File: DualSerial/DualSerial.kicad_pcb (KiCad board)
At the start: 2 copper layers, 99.9 x 99.9 mm, 22 parts, among them CN1 DB9 Male, CN2 DB9 Male, J1 COM_A_SELECT, J2 IRQ_A_SELECT, J3 COM_A_SELECT, J4 IRQ_B_SELECT, J5 Bus_ISA_8bit, U1 16550/16C550, U2 GAL16V8, U3 GD75232N, U4 1.8432 MHz, U8 16550/16C550, U9 GD75232N

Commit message: Dual Serial: Flip A and B ports to correct location.
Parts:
- J2: renamed from J4; value IRQ_B_SELECT -> IRQ_A_SELECT
- J4: renamed from J2; value IRQ_A_SELECT -> IRQ_B_SELECT
- renumbered C8 to C1, C9 to C3, C1 to C8, C3 to C9, CN2 to CN1, CN1 to CN2, U8 to U1, U9 to U3, U1 to U8, U3 to U9
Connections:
- CN1 pad 1: /SERB_PIN1 -> /SERA_PIN1
- CN1 pad 2: /SERB_PIN2 -> /SERA_PIN2
- CN1 pad 3: /SERB_PIN3 -> /SERA_PIN3
- CN1 pad 4: /SERB_PIN4 -> /SERA_PIN4
- CN1 pad 6: /SERB_PIN6 -> /SERA_PIN6
- CN1 pad 7: /SERB_PIN7 -> /SERA_PIN7
- CN1 pad 8: /SERB_PIN8 -> /SERA_PIN8
- CN1 pad 9: /SERB_PIN9 -> /SERA_PIN9
- CN2 pad 1: /SERA_PIN1 -> /SERB_PIN1
- CN2 pad 2: /SERA_PIN2 -> /SERB_PIN2
- CN2 pad 3: /SERA_PIN3 -> /SERB_PIN3
- CN2 pad 4: /SERA_PIN4 -> /SERB_PIN4
- CN2 pad 6: /SERA_PIN6 -> /SERB_PIN6
- CN2 pad 7: /SERA_PIN7 -> /SERB_PIN7
- CN2 pad 8: /SERA_PIN8 -> /SERB_PIN8
- CN2 pad 9: /SERA_PIN9 -> /SERB_PIN9
- U1 pad 14: ~UART_B_CS -> ~UART_A_CS
- U2 pad 14: ~UART_A_CS -> ~UART_B_CS
- U2 pad 15: ~UART_B_CS -> ~UART_A_CS
- U3 pad 2: /SERB_PIN9 -> /SERA_PIN9
- U3 pad 3: /SERB_PIN8 -> /SERA_PIN8
- U3 pad 4: /SERB_PIN2 -> /SERA_PIN2
- U3 pad 5: /SERB_PIN4 -> /SERA_PIN4
- U3 pad 6: /SERB_PIN3 -> /SERA_PIN3
- U3 pad 7: /SERB_PIN6 -> /SERA_PIN6
- U3 pad 8: /SERB_PIN7 -> /SERA_PIN7
- U3 pad 9: /SERB_PIN1 -> /SERA_PIN1
- U8 pad 14: ~UART_A_CS -> ~UART_B_CS
- U9 pad 2: /SERA_PIN9 -> /SERB_PIN9
- U9 pad 3: /SERA_PIN8 -> /SERB_PIN8
- U9 pad 4: /SERA_PIN2 -> /SERB_PIN2
- U9 pad 5: /SERA_PIN4 -> /SERB_PIN4
- U9 pad 6: /SERA_PIN3 -> /SERB_PIN3
- U9 pad 7: /SERA_PIN6 -> /SERB_PIN6
- U9 pad 8: /SERA_PIN7 -> /SERB_PIN7
- U9 pad 9: /SERA_PIN1 -> /SERB_PIN1
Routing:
- net ~UART_B_CS: track 8.45 -> 43.2 mm, vias 0 -> 2
- net ~UART_A_CS: track 43.2 -> 8.45 mm, vias 2 -> 0
- net /SERB_PIN2: track 24.7 -> 30.1 mm, vias 0 -> 2
- net /SERA_PIN2: track 30.1 -> 24.7 mm, vias 2 -> 0
- net /SERB_PIN8: track 17.9 -> 23.0 mm
- net /SERA_PIN8: track 23.0 -> 17.9 mm
- net /SERB_PIN6: track 16.8 -> 20.5 mm, vias 0 -> 2
- net /SERA_PIN6: track 20.5 -> 16.8 mm, vias 2 -> 0
- net /SERB_PIN7: track 21.3 -> 17.6 mm, vias 2 -> 0
- net /SERA_PIN7: track 17.6 -> 21.3 mm, vias 0 -> 2
- net /SERB_PIN9: track 18.2 -> 21.8 mm
- net /SERA_PIN9: track 21.8 -> 18.2 mm
- net /SERB_PIN1: track 16.5 -> 14.9 mm
- net /SERA_PIN1: track 14.9 -> 16.5 mm
- net /SERB_PIN3: track 15.0 -> 15.8 mm
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
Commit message: Dual Serial: Minor silk screen change.
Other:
- board text added: "COM2:"

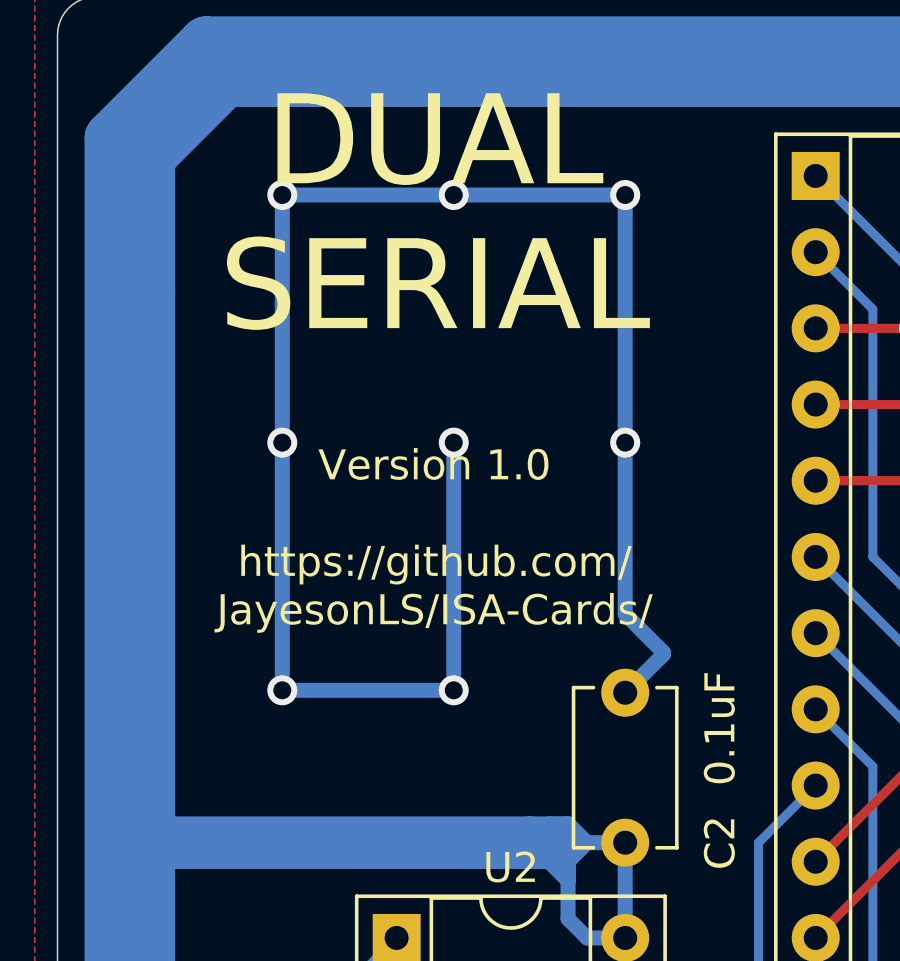
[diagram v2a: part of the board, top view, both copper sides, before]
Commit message: DualSerial: Change to ground plan vias in top left corner.
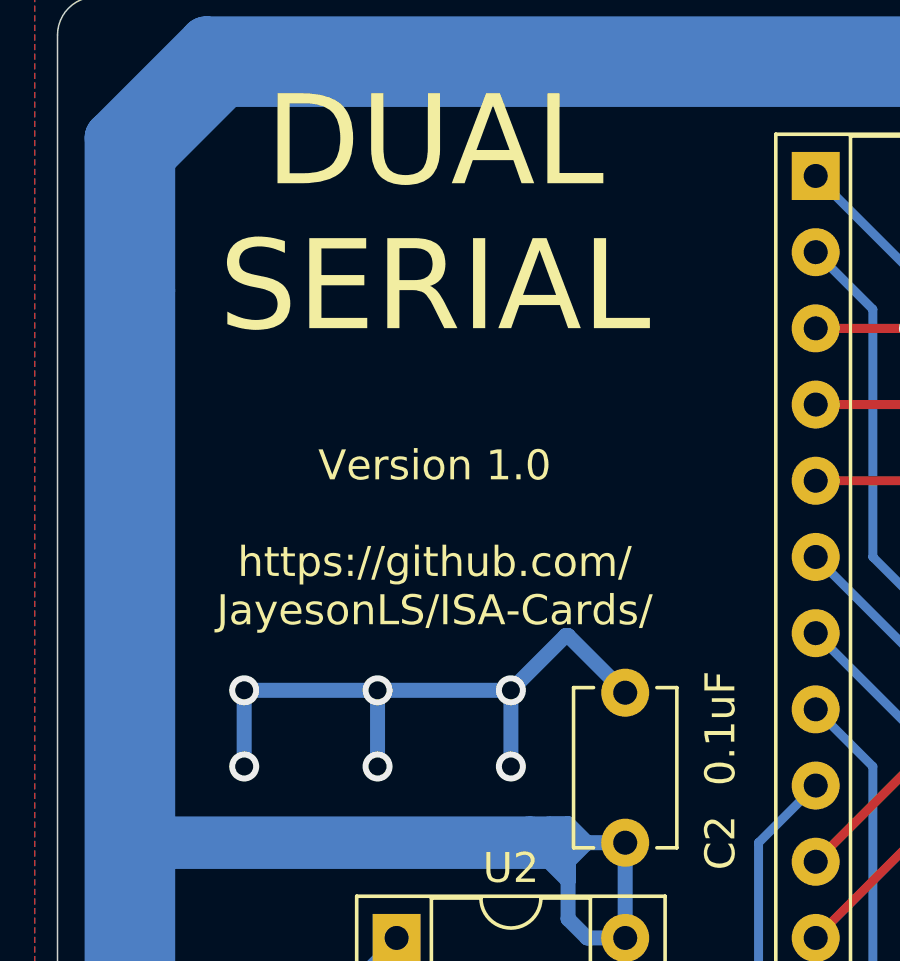
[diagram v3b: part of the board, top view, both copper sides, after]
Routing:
- net GND: track 365.0 -> 327.3 mm, vias 46 -> 44
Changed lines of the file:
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@@
     (thickness 1.6)
     (drawings 87)
-    (tracks 1197)
+    (tracks 1192)
     (zones 0)
     (modules 22)
@@
   (segment (start 173.282894 48.895) (end 170.18 48.895) (width 0.5) (layer B.Cu) (net 20))
   (segment (start 170.18 48.895) (end 166.37 48.895) (width 0.5) (layer B.Cu) (net 20))
-  (via (at 115.57 48.895) (size 1) (drill 0.6) (layers F.Cu B.Cu) (net 20))
-  (segment (start 115.57 48.895) (end 115.57 57.15) (width 0.5) (layer B.Cu) (net 20))
-  (via (at 115.57 57.15) (size 1) (drill 0.6) (layers F.Cu B.Cu) (net 20))
-  (via (at 109.855 57.15) (size 1) (drill 0.6) (layers F.Cu B.Cu) (net 20))
-  (segment (start 109.855 65.405) (end 109.855 57.15) (width 0.5) (layer B.Cu) (net 20))
-  (via (at 109.855 65.405) (size 1) (drill 0.6) (layers F.Cu B.Cu) (net 20))
-  (segment (start 115.57 48.895) (end 109.855 48.895) (width 0.5) (layer B.Cu) (net 20))
-  (via (at 109.855 48.895) (size 1) (drill 0.6) (layers F.Cu B.Cu) (net 20))
-  (segment (start 109.855 48.895) (end 104.14 48.895) (width 0.5) (layer B.Cu) (net 20))
-  (via (at 104.14 48.895) (size 1) (drill 0.6) (layers F.Cu B.Cu) (net 20))
-  (segment (start 104.14 48.895) (end 104.14 57.15) (width 0.5) (layer B.Cu) (net 20))
-  (via (at 104.14 57.15) (size 1) (drill 0.6) (layers F.Cu B.Cu) (net 20))
-  (segment (start 104.14 57.15) (end 104.14 65.405) (width 0.5) (layer B.Cu) (net 20))
-  (segment (start 104.14 65.405) (end 109.855 65.405) (width 0.5) (layer B.Cu) (net 20))
-  (via (at 104.14 65.405) (size 1) (drill 0.6) (layers F.Cu B.Cu) (net 20))
   (segment (start 140.97 53.26) (end 139.78 52.07) (width 0.5) (layer F.Cu) (net 20))
   (segment (start 140.97 53.26) (end 142.16 52.07) (width 0.5) (layer F.Cu) (net 20))
@@
   (segment (start 175.26 54.61) (end 169.545 54.61) (width 0.5) (layer B.Cu) (net 20))
   (segment (start 169.545 54.61) (end 165.1 54.61) (width 0.5) (layer B.Cu) (net 20))
-  (segment (start 115.57 65.485) (end 116.84 64.215) (width 0.5) (layer B.Cu) (net 20))
-  (segment (start 116.84 64.215) (end 116.84 64.135) (width 0.5) (layer B.Cu) (net 20))
-  (segment (start 116.84 64.135) (end 115.57 62.865) (width 0.5) (layer B.Cu) (net 20))
-  (segment (start 115.57 57.15) (end 115.57 62.865) (width 0.5) (layer B.Cu) (net 20))
   (via (at 151.765 64.77) (size 1) (drill 0.6) (layers F.Cu B.Cu) (net 20))
   (segment (start 147.955 64.77) (end 151.765 64.77) (width 0.5) (layer B.Cu) (net 20))
@@
   (segment (start 107.95 100.965) (end 105.41 100.965) (width 0.5) (layer F.Cu) (net 20))
   (segment (start 115.57 107.315) (end 115.57 109.855) (width 0.3) (layer F.Cu) (net 20))
+  (via (at 102.87 65.405) (size 1) (drill 0.6) (layers F.Cu B.Cu) (net 20))
+  (segment (start 113.665 63.58) (end 115.57 65.485) (width 0.5) (layer B.Cu) (net 20))
+  (segment (start 113.585 63.58) (end 113.665 63.58) (width 0.5) (layer B.Cu) (net 20))
+  (segment (start 111.76 65.405) (end 113.585 63.58) (width 0.5) (layer B.Cu) (net 20))
+  (via (at 111.76 65.405) (size 1) (drill 0.6) (layers F.Cu B.Cu) (net 20))
+  (segment (start 107.315 65.405) (end 111.76 65.405) (width 0.5) (layer B.Cu) (net 20))
+  (segment (start 102.87 65.405) (end 107.315 65.405) (width 0.5) (layer B.Cu) (net 20))
+  (via (at 107.315 65.405) (size 1) (drill 0.6) (layers F.Cu B.Cu) (net 20))
+  (via (at 111.76 67.945) (size 1) (drill 0.6) (layers F.Cu B.Cu) (net 20))
+  (segment (start 111.76 65.405) (end 111.76 67.945) (width 0.5) (layer B.Cu) (net 20))
+  (via (at 107.315 67.945) (size 1) (drill 0.6) (layers F.Cu B.Cu) (net 20))
+  (segment (start 107.315 65.405) (end 107.315 67.945) (width 0.5) (layer B.Cu) (net 20))
+  (via (at 102.87 67.945) (size 1) (drill 0.6) (layers F.Cu B.Cu) (net 20))
+  (segment (start 102.87 65.405) (end 102.87 67.945) (width 0.5) (layer B.Cu) (net 20))
   (segment (start 104.14 138.43) (end 104.14 128.905) (width 1.75) (layer B.Cu) (net 21))
   (segment (start 99.695 47.625) (end 102.235 45.085) (width 1.75) (layer B.Cu) (net 21))
